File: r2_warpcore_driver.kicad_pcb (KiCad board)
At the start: 2 copper layers, 151 x 94.4 mm, 55 parts, among them J1 Conn_01x04_Pin, J10 Screw_Terminal_01x02, J11 Conn_01x03_Pin, J13 Conn_01x14_Pin, J14 Conn_01x05_Pin, J15 Conn_01x03_Pin, J16 Conn_01x03_Pin, J2 Conn_01x03_Pin, J3 Conn_01x03_Pin, J4 Conn_01x04_Pin, J5 Screw_Terminal_01x04, J6 Conn_01x05_Pin, J7 Screw_Terminal_01x04, J8 Screw_Terminal_01x04, J9 Screw_Terminal_01x03, Q1 L8050QLT1G, Q2 L8050QLT1G, Q3 IRLB8721PBF, Q4 IRLB8721PBF, Q5 IRLB8721PBF, Q6 Q_PNP_BEC, Q7 Q_PNP_BEC, Q8 Q_PNP_BEC, SW1 SW_Push, SW2 SW_Push, U1 ESP32-S3-MINI-1, U2 LDL1117S33R

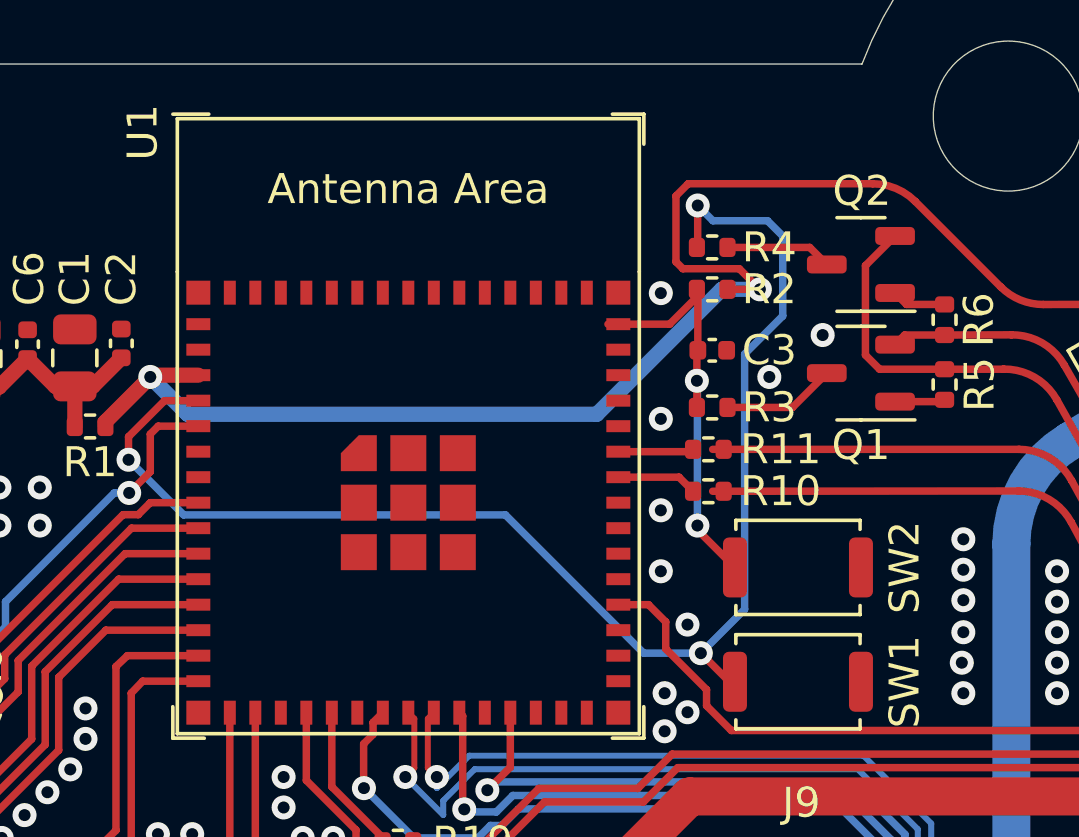
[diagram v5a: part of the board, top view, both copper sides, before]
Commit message: Adjusting some traces
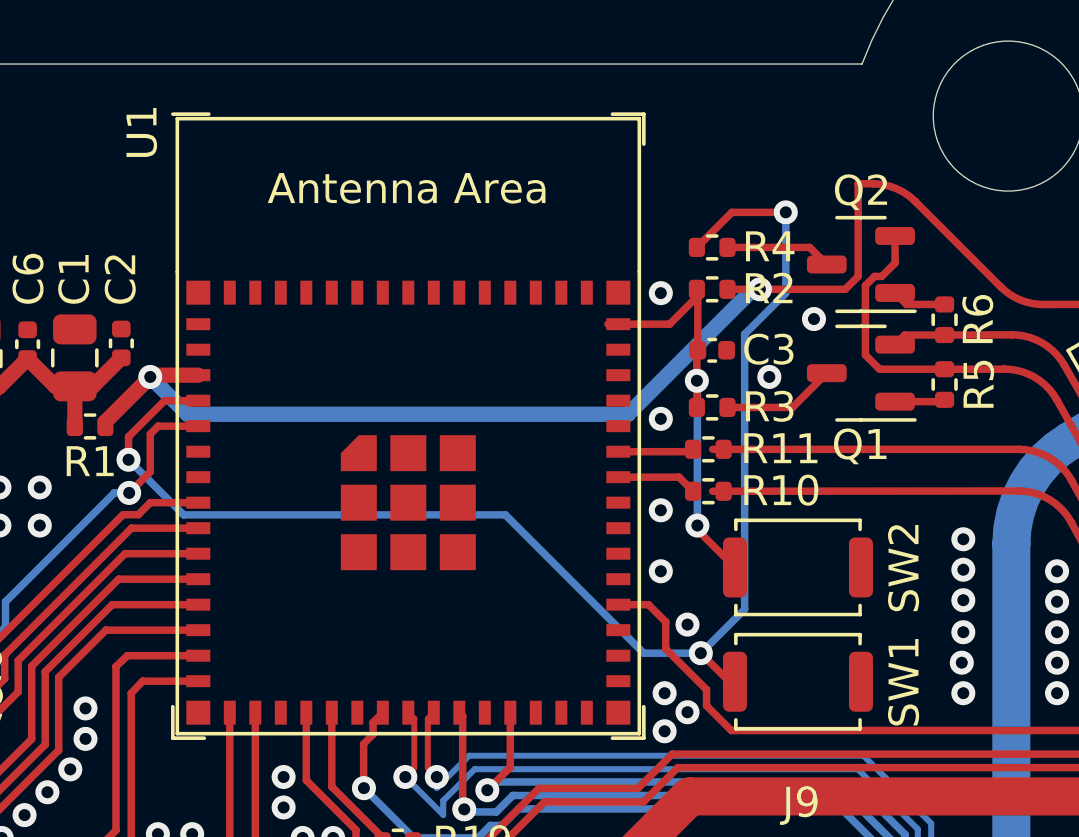
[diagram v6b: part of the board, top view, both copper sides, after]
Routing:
- net /ESP_3V3: track 114.6 -> 109.5 mm
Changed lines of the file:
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@@
   (via (at 150.622 69.469) (size 0.8) (drill 0.4) (layers "F.Cu" "B.Cu") (free) (net 1))
   (via (at 182.626 56.642) (size 0.8) (drill 0.4) (layers "F.Cu" "B.Cu") (free) (net 1))
-  (via (at 171.638 52.832) (size 0.8) (drill 0.4) (layers "F.Cu" "B.Cu") (free) (net 1))
+  (via (at 171.3484 52.2986) (size 0.8) (drill 0.4) (layers "F.Cu" "B.Cu") (free) (net 1))
   (via (at 160.401 72.771) (size 0.8) (drill 0.4) (layers "F.Cu" "B.Cu") (free) (net 1))
   (via (at 153.67 68.58) (size 0.8) (drill 0.4) (layers "F.Cu" "B.Cu") (free) (net 1))
@@
   (segment (start 175.702 51.812) (end 174.433 51.812) (width 0.25) (layer "F.Cu") (net 29))
   (segment (start 174.433 51.812) (end 174.051 51.43) (width 0.25) (layer "F.Cu") (net 29))
+  (segment (start 173.0635 51.18233) (end 173.36783 50.878) (width 0.25) (layer "F.Cu") (net 30))
+  (segment (start 173.0635 53.498751) (end 173.0635 51.18233) (width 0.25) (layer "F.Cu") (net 30))
   (segment (start 175.702 53.971) (end 177.664811 53.971) (width 0.25) (layer "F.Cu") (net 30))
+  (segment (start 175.702 53.971) (end 173.535749 53.971) (width 0.25) (layer "F.Cu") (net 30))
   (segment (start 181.852558 59.291447) (end 179.443072 54.989633) (width 0.25) (layer "F.Cu") (net 30))
-  (segment (start 173.0635 50.5175) (end 174.051 49.53) (width 0.25) (layer "F.Cu") (net 30))
-  (segment (start 175.702 53.971) (end 173.535749 53.971) (width 0.25) (layer "F.Cu") (net 30))
   (segment (start 177.664811 53.971) (end 177.668608 53.967203) (width 0.25) (layer "F.Cu") (net 30))
+  (segment (start 173.36783 50.878) (end 173.6072 50.878) (width 0.25) (layer "F.Cu") (net 30))
+  (segment (start 187.893 60.30681) (end 183.599776 60.314094) (width 0.25) (layer "F.Cu") (net 30))
+  (segment (start 174.051 50.4342) (end 174.051 49.53) (width 0.25) (layer "F.Cu") (net 30))
+  (segment (start 173.6072 50.878) (end 174.051 50.4342) (width 0.25) (layer "F.Cu") (net 30))
   (segment (start 173.535749 53.971) (end 173.0635 53.498751) (width 0.25) (layer "F.Cu") (net 30))
-  (segment (start 187.893 60.30681) (end 183.599776 60.314094) (width 0.25) (layer "F.Cu") (net 30))
-  (segment (start 173.0635 53.498751) (end 173.0635 50.5175) (width 0.25) (layer "F.Cu") (net 30))
   (arc (start 177.668608 53.967203) (mid 178.696634 54.234065) (end 179.443072 54.989633) (width 0.25) (layer "F.Cu") (net 30))
   (arc (start 181.852558 59.291447) (mid 182.587215 60.040174) (end 183.599776 60.314094) (width 0.25) (layer "F.Cu") (net 30))
   (segment (start 171.207 49.911) (end 171.776 50.48) (width 0.25) (layer "F.Cu") (net 31))
   (segment (start 168.465 49.911) (end 171.207 49.911) (width 0.25) (layer "F.Cu") (net 31))
-  (segment (start 167.4724 48.514) (end 167.4724 49.8836) (width 0.25) (layer "F.Cu") (net 32))
+  (segment (start 168.6134 48.7426) (end 167.4724 49.8836) (width 0.25) (layer "F.Cu") (net 32))
+  (segment (start 170.4086 48.7426) (end 168.6134 48.7426) (width 0.25) (layer "F.Cu") (net 32))
   (segment (start 148.5 56.989361) (end 148.5 56.222604) (width 0.25) (layer "F.Cu") (net 32))
   (segment (start 148.5 56.222604) (end 149.702604 55.02) (width 0.25) (layer "F.Cu") (net 32))
@@
   (via (at 167.5765 63.4365) (size 0.8) (drill 0.4) (layers "F.Cu" "B.Cu") (net 32))
   (via (at 148.5 56.989361) (size 0.8) (drill 0.4) (layers "F.Cu" "B.Cu") (free) (net 32))
-  (via (at 167.4724 48.514) (size 0.8) (drill 0.4) (layers "F.Cu" "B.Cu") (net 32))
-  (segment (start 169.799 49.022) (end 167.9804 49.022) (width 0.25) (layer "B.Cu") (net 32))
-  (segment (start 170.307 52.197) (end 170.307 49.53) (width 0.25) (layer "B.Cu") (net 32))
-  (segment (start 169.037 61.976) (end 169.037 53.467) (width 0.25) (layer "B.Cu") (net 32))
+  (via (at 170.4086 48.7426) (size 0.8) (drill 0.4) (layers "F.Cu" "B.Cu") (net 32))
+  (segment (start 170.4086 48.7426) (end 170.4086 51.435) (width 0.25) (layer "B.Cu") (net 32))
+  (segment (start 169.037 52.8066) (end 169.037 61.976) (width 0.25) (layer "B.Cu") (net 32))
+  (segment (start 170.4086 51.435) (end 169.037 52.8066) (width 0.25) (layer "B.Cu") (net 32))
   (segment (start 150.337039 58.8264) (end 148.5 56.989361) (width 0.25) (layer "B.Cu") (net 32))
   (segment (start 167.5765 63.4365) (end 165.6715 63.4365) (width 0.25) (layer "B.Cu") (net 32))
-  (segment (start 167.9804 49.022) (end 167.4724 48.514) (width 0.25) (layer "B.Cu") (net 32))
-  (segment (start 169.037 53.467) (end 170.307 52.197) (width 0.25) (layer "B.Cu") (net 32))
-  (segment (start 170.307 49.53) (end 169.799 49.022) (width 0.25) (layer "B.Cu") (net 32))
-  (segment (start 167.5765 63.4365) (end 169.037 61.976) (width 0.25) (layer "B.Cu") (net 32))
+  (segment (start 169.037 61.976) (end 167.5765 63.4365) (width 0.25) (layer "B.Cu") (net 32))
   (segment (start 165.6715 63.4365) (end 161.0614 58.8264) (width 0.25) (layer "B.Cu") (net 32))
   (segment (start 161.0614 58.8264) (end 150.337039 58.8264) (width 0.25) (layer "B.Cu") (net 32))
@@
   (segment (start 203.9874 87.3506) (end 203.454 87.884) (width 0.25) (layer "F.Cu") (net 53))
   (segment (start 203.454 87.884) (end 203.454 101.665773) (width 0.25) (layer "F.Cu") (net 53))
-  (segment (start 178.99391 51.813883) (end 186.990576 51.793521) (width 0.25) (layer "F.Cu") (net 53))
-  (segment (start 166.9796 50.6222) (end 166.7474 50.39) (width 0.25) (layer "F.Cu") (net 53))
-  (segment (start 167.156 47.789) (end 173.307073 47.789) (width 0.25) (layer "F.Cu") (net 53))
   (segment (start 203.454 101.665773) (end 201.650591 103.469182) (width 0.25) (layer "F.Cu") (net 53))
   (segment (start 147.7284 55.7256) (end 149.225 54.229) (width 0.508) (layer "F.Cu") (net 53))
   (segment (start 169.545 51.308) (end 168.465 51.308) (width 0.25) (layer "F.Cu") (net 53))
-  (segment (start 169.545 51.308) (end 168.8592 50.6222) (width 0.25) (layer "F.Cu") (net 53))
+  (segment (start 172.3898 51.308) (end 172.8216 50.8762) (width 0.25) (layer "F.Cu") (net 53))
   (segment (start 149.225 54.229) (end 149.284 54.17) (width 0.508) (layer "F.Cu") (net 53))
+  (segment (start 172.8216 47.789) (end 173.307073 47.789) (width 0.25) (layer "F.Cu") (net 53))
   (segment (start 174.721286 48.374786) (end 177.574603 51.228103) (width 0.25) (layer "F.Cu") (net 53))
-  (segment (start 166.7474 50.39) (end 166.7474 48.1976) (width 0.25) (layer "F.Cu") (net 53))
+  (segment (start 169.545 51.308) (end 172.3898 51.308) (width 0.25) (layer "F.Cu") (net 53))
+  (segment (start 188.719502 52.779414) (end 206.9084 84.4042) (width 0.25) (layer "F.Cu") (net 53))
   (segment (start 149.284 54.17) (end 150.82637 54.17) (width 0.508) (layer "F.Cu") (net 53))
+  (segment (start 172.8216 50.8762) (end 172.8216 47.789) (width 0.25) (layer "F.Cu") (net 53))
   (segment (start 147.7284 55.88) (end 147.7284 55.7256) (width 0.508) (layer "F.Cu") (net 53))
-  (segment (start 188.719502 52.779414) (end 206.9084 84.4042) (width 0.25) (layer "F.Cu") (net 53))
-  (segment (start 166.7474 48.1976) (end 167.156 47.789) (width 0.25) (layer "F.Cu") (net 53))
-  (segment (start 168.8592 50.6222) (end 166.9796 50.6222) (width 0.25) (layer "F.Cu") (net 53))
+  (segment (start 178.99391 51.813883) (end 186.990576 51.793521) (width 0.25) (layer "F.Cu") (net 53))
   (via (at 203.9874 87.3506) (size 0.8) (drill 0.4) (layers "F.Cu" "B.Cu") (net 53))
   (via (at 149.225 54.229) (size 0.8) (drill 0.4) (layers "F.Cu" "B.Cu") (free) (net 53))
   (via (at 206.9084 84.4042) (size 0.8) (drill 0.4) (layers "F.Cu" "B.Cu") (net 53))
   (via (at 169.545 51.308) (size 0.8) (drill 0.4) (layers "F.Cu" "B.Cu") (net 53))
+  (arc (start 186.990576 51.793521) (mid 187.986382 52.056135) (end 188.719502 52.779414) (width 0.25) (layer "F.Cu") (net 53))
   (arc (start 173.307073 47.789) (mid 174.07244 47.941241) (end 174.721286 48.374786) (width 0.25) (layer "F.Cu") (net 53))
   (arc (start 177.574603 51.228103) (mid 178.225803 51.662622) (end 178.99391 51.813883) (width 0.25) (layer "F.Cu") (net 53))
-  (arc (start 186.990576 51.793521) (mid 187.986382 52.056135) (end 188.719502 52.779414) (width 0.25) (layer "F.Cu") (net 53))
-  (segment (start 164.1094 55.4736) (end 168.275 51.308) (width 0.508) (layer "B.Cu") (net 53))
+  (segment (start 149.225 54.229) (end 150.4696 55.4736) (width 0.508) (layer "B.Cu") (net 53))
+  (segment (start 165.1508 55.4736) (end 169.3164 51.308) (width 0.508) (layer "B.Cu") (net 53))
+  (segment (start 150.4696 55.4736) (end 165.1508 55.4736) (width 0.508) (layer "B.Cu") (net 53))
   (segment (start 203.9874 87.3506) (end 206.9084 84.4296) (width 0.25) (layer "B.Cu") (net 53))
   (segment (start 206.9084 84.4296) (end 206.9084 84.4042) (width 0.25) (layer "B.Cu") (net 53))
-  (segment (start 168.275 51.308) (end 169.545 51.308) (width 0.508) (layer "B.Cu") (net 53))
-  (segment (start 150.4696 55.4736) (end 164.1094 55.4736) (width 0.508) (layer "B.Cu") (net 53))
-  (segment (start 149.225 54.229) (end 150.4696 55.4736) (width 0.508) (layer "B.Cu") (net 53))
+  (segment (start 169.3164 51.308) (end 169.545 51.308) (width 0.508) (layer "B.Cu") (net 53))
   (segment (start 192.913 85.09) (end 192.913 121.4374) (width 1.27) (layer "F.Cu") (net 54))
   (segment (start 177.927 71.374) (end 179.197 71.374) (width 1.27) (layer "F.Cu") (net 54))

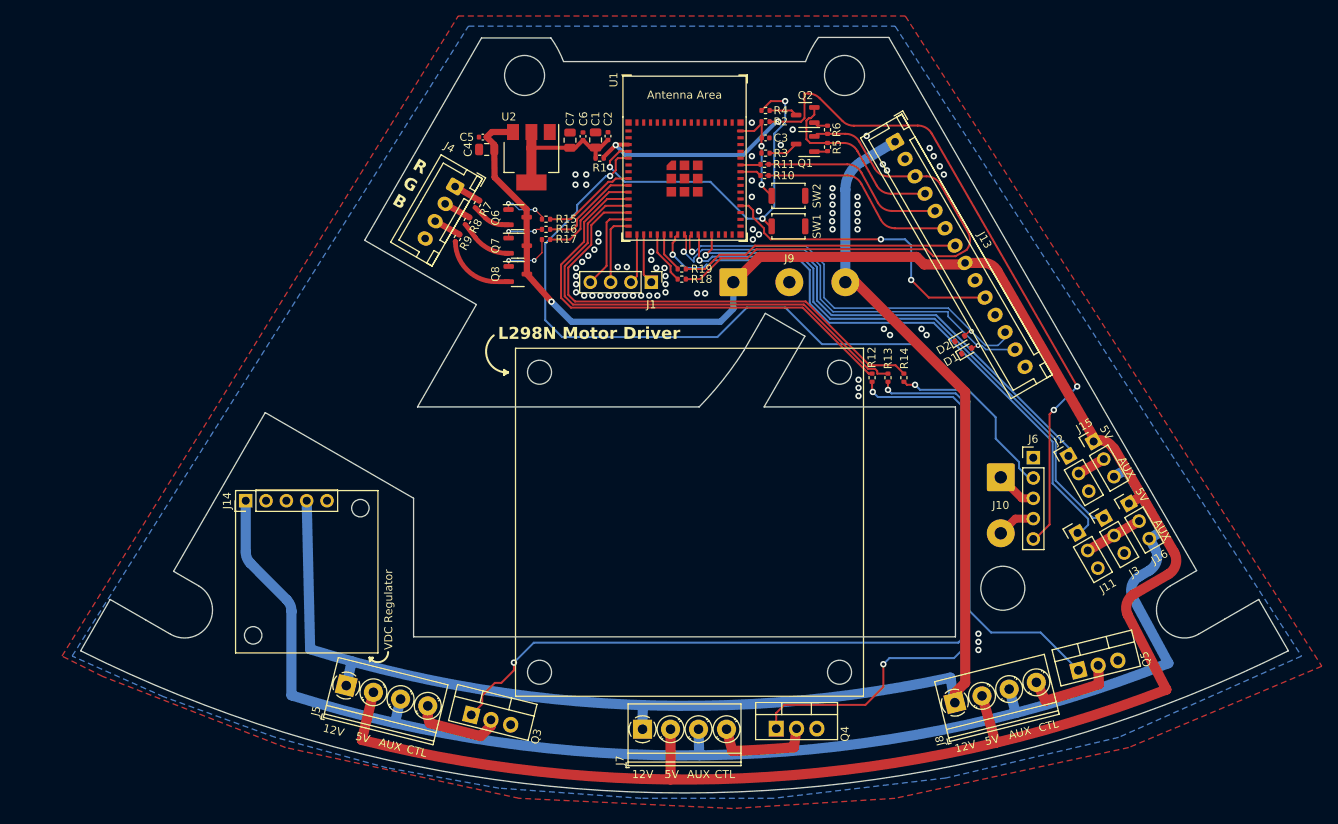
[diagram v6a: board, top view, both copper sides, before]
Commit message: Updates to set up USB traces, and to make it a 4-layer board.
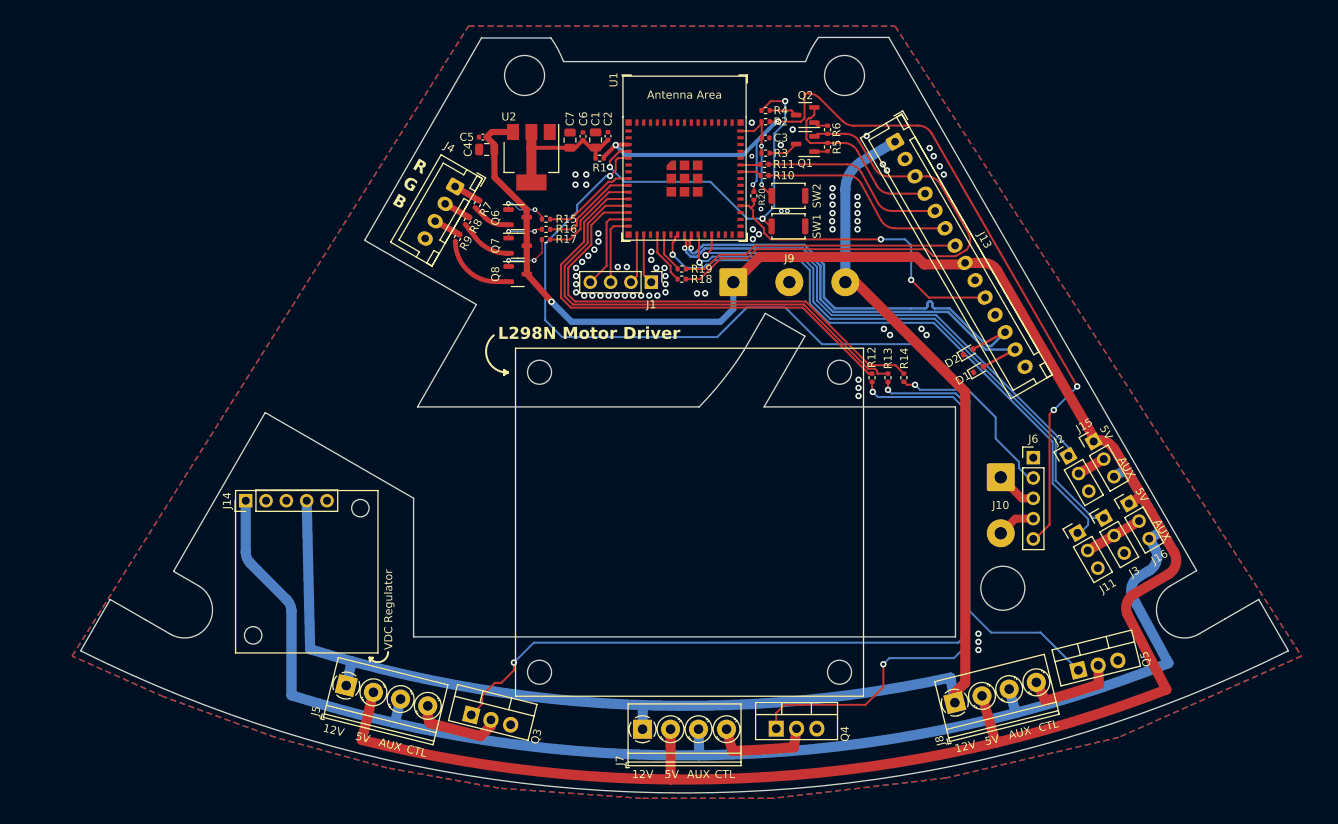
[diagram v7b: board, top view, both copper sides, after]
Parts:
- added R20: 1K(1%), Resistor_SMD:R_0402_1005Metric, F.Cu at (166.5, 60.6)
- moved D1 2.76 mm to (194.6, 82.3)
- moved D2 1.97 mm to (193.3, 80.1)
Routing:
- net /ESP_3V3: track 109.5 -> 116.0 mm, vias 4 -> 5
- net /D+: track 51.3 -> 56.4 mm, vias 2 -> 1
- net /D-: track 54.0 -> 56.4 mm, vias 2 -> 1
- net /ID: track 38.7 -> 39.9 mm
- added copper zone on In1.Cu, net GND
- added copper zone on In2.Cu, net GND
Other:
- copper layers 2 -> 4
- rule solder_mask_min_width: 0.12 -> 0.1016
